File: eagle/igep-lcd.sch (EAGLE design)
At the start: 66 parts, among them IC1 LM1117IMPX-3.3, U1 SN74LVC8T245PW, U2 SN74LVC8T245PW, U3 SN74LVC8T245PW, U4 SN74LVC8T245PW

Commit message: Fixed one forgotten capacitor
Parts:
- removed C12: 0.1uF, rcl:C-EU050-025X075
- added C1: 100nF, rcl:C-EUC1206
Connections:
- net N$2: now also C1.2; no longer C12.2
- net N$3: now also C1.1; no longer C12.1
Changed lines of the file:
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@@
 <part name="U$5" library="lcd-bl" deviceset="LCD_BL" device=""/>
 <part name="U$6" library="ads7843" deviceset="ADS7843" device=""/>
-<part name="C12" library="rcl" deviceset="C-EU" device="050-025X075" value="0.1uF"/>
 <part name="C40" library="rcl" deviceset="C-EU" device="C1206" value="100nF"/>
 <part name="C16" library="rcl" deviceset="C-EU" device="C1206" value="100nF"/>
@@
 <part name="C11" library="rcl" deviceset="C-EU" device="C1206" value="10uF"/>
 <part name="C2" library="rcl" deviceset="C-EU" device="C1206" value="22uF"/>
+<part name="C1" library="rcl" deviceset="C-EU" device="C1206" value="100nF"/>
 </parts>
 <sheets>
@@
 <instance part="U$5" gate="G$1" x="208.28" y="-231.14" rot="MR270"/>
 <instance part="U$6" gate="G$1" x="106.68" y="-350.52"/>
-<instance part="C12" gate="G$1" x="132.08" y="121.92"/>
 <instance part="C40" gate="G$1" x="203.2" y="127" rot="R90"/>
 <instance part="C16" gate="G$1" x="205.74" y="124.46" rot="R90"/>
@@
 <instance part="C11" gate="G$1" x="48.26" y="71.12"/>
 <instance part="C2" gate="G$1" x="66.04" y="71.12"/>
+<instance part="C1" gate="G$1" x="132.08" y="121.92"/>
 </instances>
 <busses>
@@
 <wire x1="320.04" y1="81.28" x2="289.56" y2="81.28" width="0.1524" layer="91"/>
 <junction x="289.56" y="81.28"/>
-<pinref part="C12" gate="G$1" pin="1"/>
-<junction x="132.08" y="124.46"/>
 <pinref part="C39" gate="G$1" pin="1"/>
 <junction x="132.08" y="-5.08"/>
@@
 <junction x="132.08" y="60.96"/>
 <pinref part="C2" gate="G$1" pin="1"/>
+<pinref part="C1" gate="G$1" pin="1"/>
+<junction x="132.08" y="124.46"/>
 </segment>
 </net>
@@
 <wire x1="134.62" y1="35.56" x2="132.08" y2="35.56" width="0.1524" layer="91"/>
 <wire x1="132.08" y1="35.56" x2="132.08" y2="53.34" width="0.1524" layer="91"/>
-<pinref part="C12" gate="G$1" pin="2"/>
 <wire x1="134.62" y1="99.06" x2="132.08" y2="99.06" width="0.1524" layer="91"/>
 <wire x1="132.08" y1="99.06" x2="132.08" y2="116.84" width="0.1524" layer="91"/>
@@
 <pinref part="C11" gate="G$1" pin="2"/>
 <pinref part="C2" gate="G$1" pin="2"/>
-</segment>
-</net>
+<pinref part="C1" gate="G$1" pin="2"/>
+</segment>
+</net>

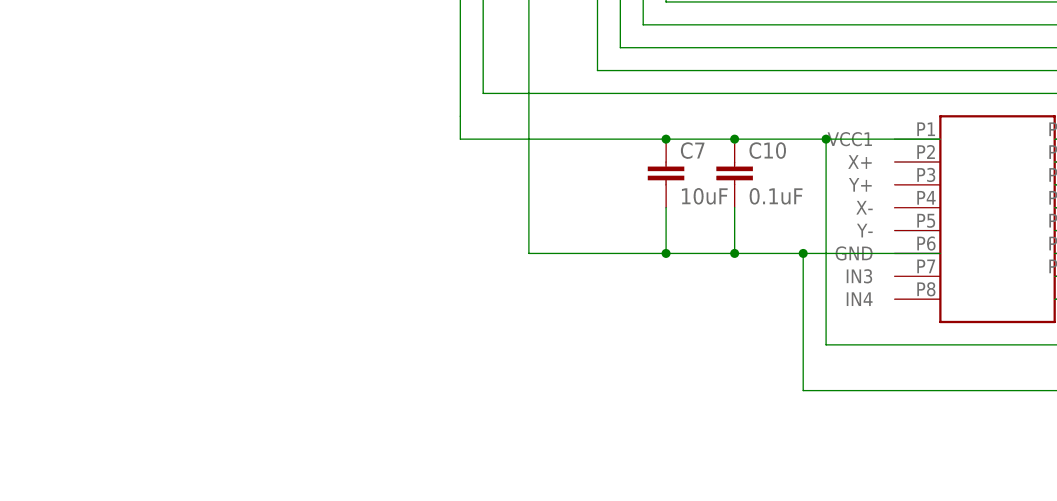
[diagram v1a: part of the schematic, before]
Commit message: Added TS connector eagle library Added TS connector to the schematic
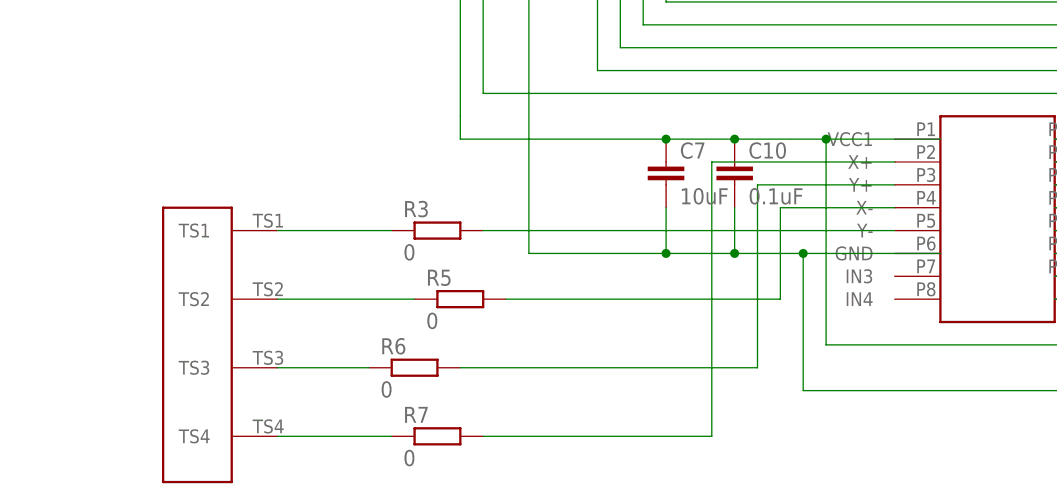
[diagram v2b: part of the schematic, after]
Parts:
- added R3, R5, R6, R7: 0, rcl:R-EU_R1206
- added U$7: TS_CON, ts_con:TS_CON
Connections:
- new net N$12: R3.2
- new net N$29: R3.1, U$7.TS1
- new net N$30: R5.2
- new net N$31: R5.1, U$7.TS2
- new net N$32: R6.2
- new net N$33: R6.1, U$7.TS3
- new net N$34: R7.1, U$7.TS4
- new net N$35: R7.2
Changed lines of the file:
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@@
 <part name="C2" library="rcl" deviceset="C-EU" device="C1206" value="22uF"/>
 <part name="C1" library="rcl" deviceset="C-EU" device="C1206" value="100nF"/>
+<part name="U$7" library="ts_con" deviceset="TS_CON" device=""/>
+<part name="R3" library="rcl" deviceset="R-EU_" device="R1206" value="0"/>
+<part name="R5" library="rcl" deviceset="R-EU_" device="R1206" value="0"/>
+<part name="R6" library="rcl" deviceset="R-EU_" device="R1206" value="0"/>
+<part name="R7" library="rcl" deviceset="R-EU_" device="R1206" value="0"/>
 </parts>
 <sheets>
@@
 <instance part="C2" gate="G$1" x="66.04" y="71.12"/>
 <instance part="C1" gate="G$1" x="132.08" y="121.92"/>
+<instance part="U$7" gate="G$1" x="17.78" y="-373.38" rot="R270"/>
+<instance part="R3" gate="G$1" x="43.18" y="-347.98"/>
+<instance part="R5" gate="G$1" x="45.72" y="-355.6"/>
+<instance part="R6" gate="G$1" x="40.64" y="-363.22"/>
+<instance part="R7" gate="G$1" x="43.18" y="-370.84"/>
 </instances>
 <busses>
@@
 </segment>
 </net>
+<net name="N$12" class="0">
+<segment>
+<wire x1="93.98" y1="-347.98" x2="48.26" y2="-347.98" width="0.1524" layer="91"/>
+<pinref part="R3" gate="G$1" pin="2"/>
+</segment>
+</net>
+<net name="N$29" class="0">
+<segment>
+<pinref part="U$7" gate="G$1" pin="TS1"/>
+<pinref part="R3" gate="G$1" pin="1"/>
+<wire x1="38.1" y1="-347.98" x2="25.4" y2="-347.98" width="0.1524" layer="91"/>
+</segment>
+</net>
+<net name="N$30" class="0">
+<segment>
+<wire x1="93.98" y1="-345.44" x2="81.28" y2="-345.44" width="0.1524" layer="91"/>
+<wire x1="81.28" y1="-345.44" x2="81.28" y2="-355.6" width="0.1524" layer="91"/>
+<wire x1="81.28" y1="-355.6" x2="50.8" y2="-355.6" width="0.1524" layer="91"/>
+<pinref part="R5" gate="G$1" pin="2"/>
+</segment>
+</net>
+<net name="N$31" class="0">
+<segment>
+<pinref part="U$7" gate="G$1" pin="TS2"/>
+<wire x1="40.64" y1="-355.6" x2="25.4" y2="-355.6" width="0.1524" layer="91"/>
+<pinref part="R5" gate="G$1" pin="1"/>
+</segment>
+</net>
+<net name="N$32" class="0">
+<segment>
+<wire x1="93.98" y1="-342.9" x2="78.74" y2="-342.9" width="0.1524" layer="91"/>
+<wire x1="78.74" y1="-342.9" x2="78.74" y2="-363.22" width="0.1524" layer="91"/>
+<wire x1="78.74" y1="-363.22" x2="45.72" y2="-363.22" width="0.1524" layer="91"/>
+<pinref part="R6" gate="G$1" pin="2"/>
+</segment>
+</net>
+<net name="N$33" class="0">
+<segment>
+<pinref part="U$7" gate="G$1" pin="TS3"/>
+<pinref part="R6" gate="G$1" pin="1"/>
+<wire x1="25.4" y1="-363.22" x2="35.56" y2="-363.22" width="0.1524" layer="91"/>
+</segment>
+</net>
+<net name="N$34" class="0">
+<segment>
+<pinref part="U$7" gate="G$1" pin="TS4"/>
+<pinref part="R7" gate="G$1" pin="1"/>
+<wire x1="25.4" y1="-370.84" x2="38.1" y2="-370.84" width="0.1524" layer="91"/>
+</segment>
+</net>
+<net name="N$35" class="0">
+<segment>
+<wire x1="93.98" y1="-340.36" x2="73.66" y2="-340.36" width="0.1524" layer="91"/>
+<wire x1="73.66" y1="-340.36" x2="73.66" y2="-370.84" width="0.1524" layer="91"/>
+<pinref part="R7" gate="G$1" pin="2"/>
+<wire x1="73.66" y1="-370.84" x2="48.26" y2="-370.84" width="0.1524" layer="91"/>
+</segment>
+</net>

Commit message: Added lcd connector Fix connections @ schema
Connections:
- removed net N$35 (its old number): R7.2
- new net N$3: R7.2, U$6.X+
- net N$1: now also U$1.MCSPI1_CLK
- net N$12: now also U$6.Y-
- net N$30: now also U$6.X-
- net N$32: now also U$6.Y+
- net N$7: now also U$1.MCSPI1_CS0
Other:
- moved on the sheet: C1, C10, C13, C14, C16, C39, C40, C7

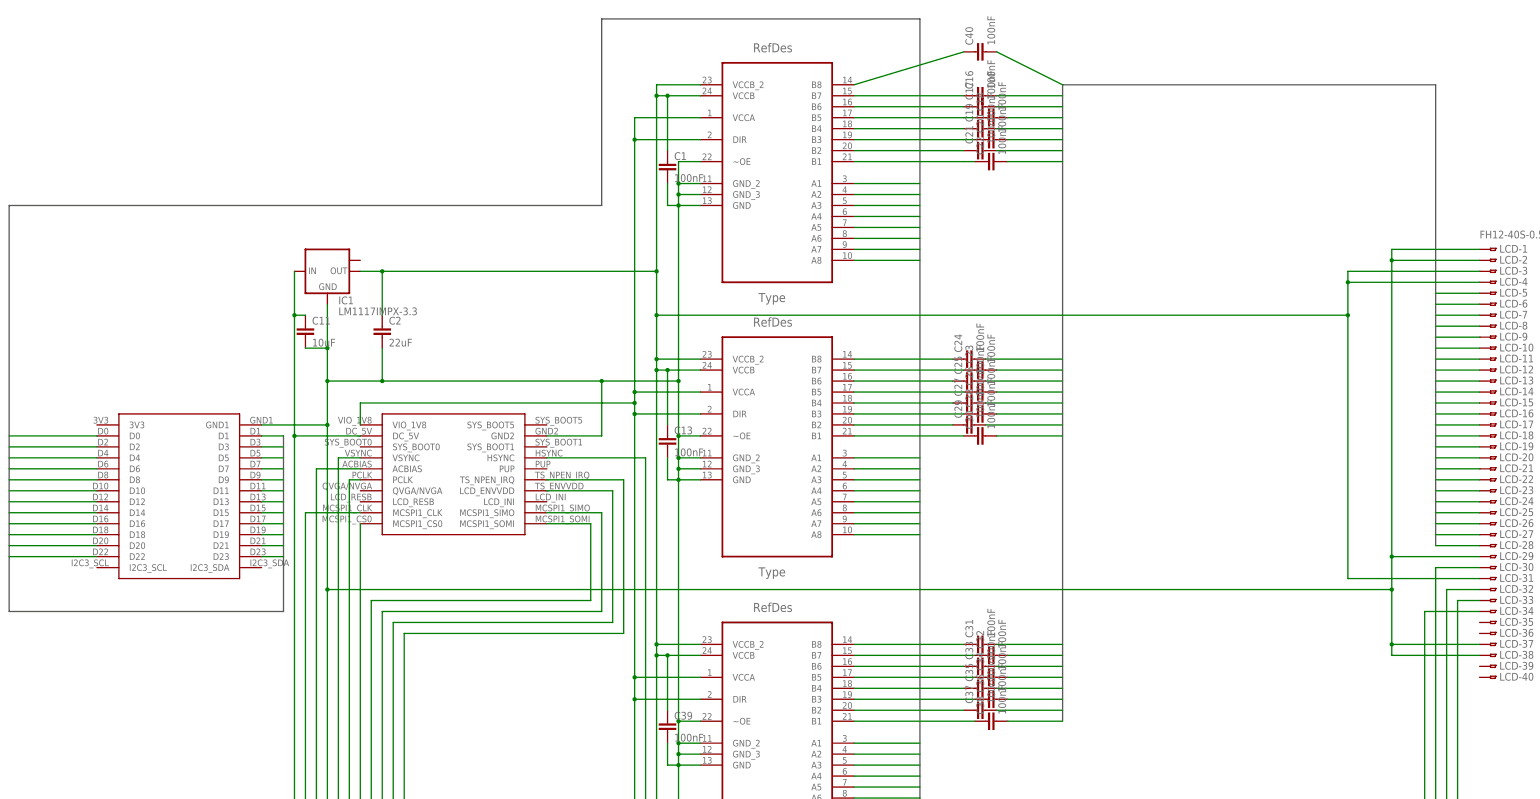
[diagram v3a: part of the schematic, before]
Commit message: Fixed ERC rules for bus
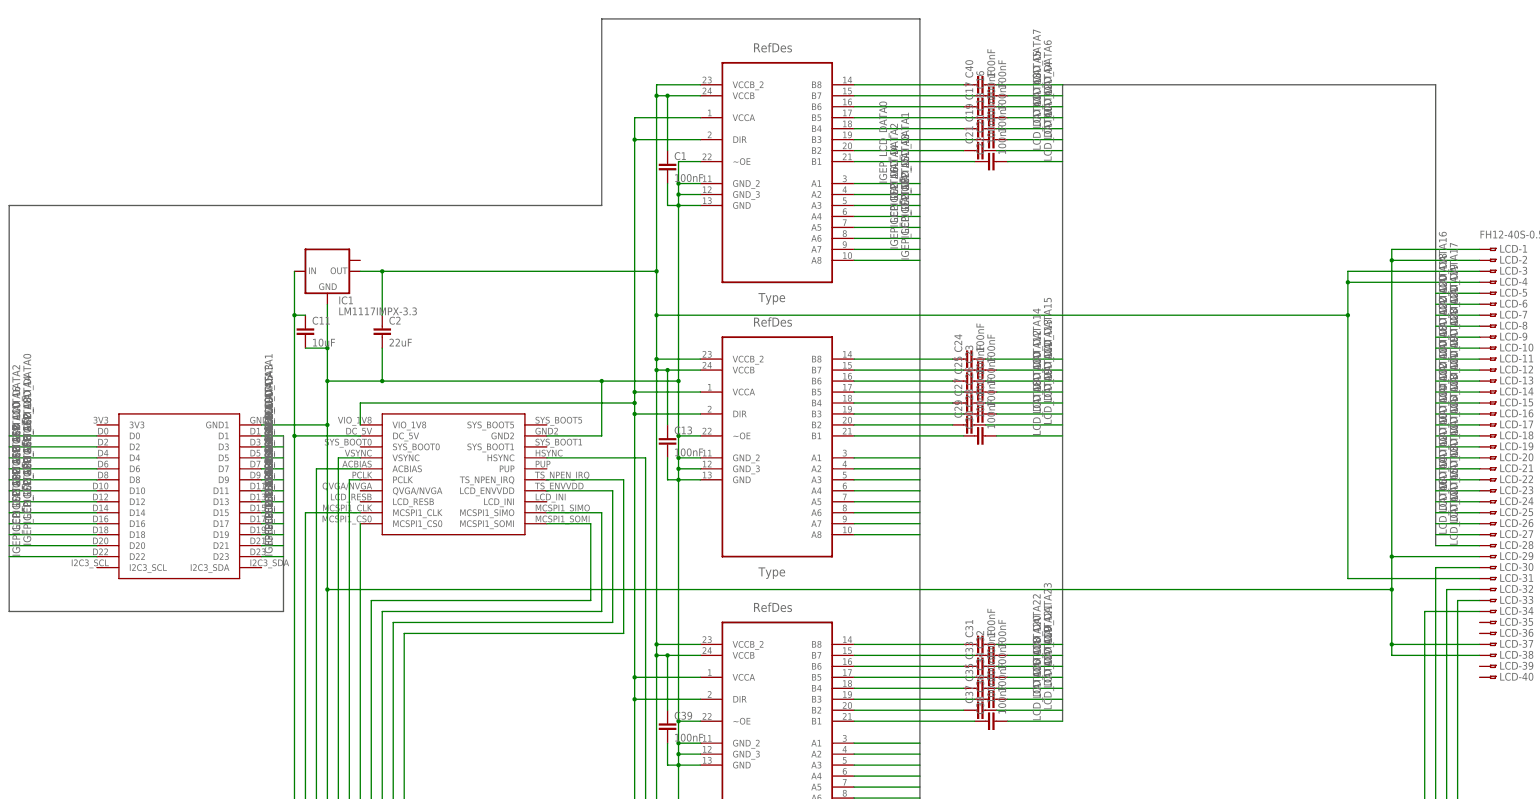
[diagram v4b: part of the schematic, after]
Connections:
- new net N$19: C40.1, U1.B8
- new net N$28: C24.1, U2.B8
- new net N$37: C16.1, U1.B7
- new net N$38: C17.1, U1.B6
- new net N$39: C18.1, U1.B5
- new net N$40: C19.1, U1.B4
- new net N$41: C20.1, U1.B3
- new net N$42: C21.1, U1.B2
- new net N$43: C22.1, U1.B1
- new net N$44: C23.1, U2.B7
- new net N$45: C25.1, U2.B6
- new net N$46: C26.1, U2.B5
- new net N$48: C28.1, U2.B3
- new net N$49: C29.1, U2.B2
- new net N$50: C30.1, U2.B1
- new net N$51: C31.1, U3.B8
- new net N$52: C32.1, U3.B7
- new net N$53: C33.1, U3.B6
- new net N$54: C34.1, U3.B5
- new net N$55: C35.1, U3.B4
- new net N$56: C36.1, U3.B3
- new net N$57: C37.1, U3.B2
- new net N$58: C38.1, U3.B1
- net LCD_DATA0: no longer C22.1, U1.B1
- net LCD_DATA1: no longer C21.1, U1.B2
- net LCD_DATA10: no longer C28.1, U2.B3
- net LCD_DATA12: no longer C26.1, U2.B5
- net LCD_DATA13: no longer C25.1, U2.B6
- net LCD_DATA14: no longer C23.1, U2.B7
- net LCD_DATA15: no longer C24.1, U2.B8
- net LCD_DATA16: no longer C38.1, U3.B1
- net LCD_DATA17: no longer C37.1, U3.B2
- net LCD_DATA18: no longer C36.1, U3.B3
- net LCD_DATA19: no longer C35.1, U3.B4
- net LCD_DATA2: no longer C20.1, U1.B3
- net LCD_DATA20: no longer C34.1, U3.B5
- net LCD_DATA21: no longer C33.1, U3.B6
- net LCD_DATA22: no longer C32.1, U3.B7
- net LCD_DATA23: no longer C31.1, U3.B8
- net LCD_DATA3: no longer C19.1, U1.B4
- net LCD_DATA4: no longer C18.1, U1.B5
- net LCD_DATA5: no longer C17.1, U1.B6
- net LCD_DATA6: no longer C16.1, U1.B7
- net LCD_DATA7: no longer C40.1, U1.B8
- net LCD_DATA8: no longer C30.1, U2.B1
- net LCD_DATA9: no longer C29.1, U2.B2
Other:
- moved on the sheet: C16, C40

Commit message: Added crosslinks on decoupling capacitors (to ease prototyping)
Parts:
- removed BL_5VOLT_1, BL_5VOLT_2, BL_5VOLT_3, BL_PWM_1, BL_PWM_2, BL_PWM_3: TPB1,27, testpad:TPB1,27
- added R10, R8, R9: 0, rcl:R-EU_R1206
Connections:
- removed net N$12: R3.2, U$6.Y-
- removed net N$18: BL_PWM_2.TP, U$3.EN
- removed net N$19: C40.1, U1.B8
- removed net N$24: BL_PWM_3.TP, U$4.EN
- removed net N$28: C24.1, U2.B8
- removed net N$3: R7.2, U$6.X+
- removed net N$30: R5.2, U$6.X-
- removed net N$32: R6.2, U$6.Y+
- removed net N$37: C16.1, U1.B7
- removed net N$38: C17.1, U1.B6
- removed net N$39: C18.1, U1.B5
- removed net N$40: C19.1, U1.B4
- removed net N$41: C20.1, U1.B3
- removed net N$42: C21.1, U1.B2
- removed net N$43: C22.1, U1.B1
- removed net N$44: C23.1, U2.B7
- removed net N$45: C25.1, U2.B6
- removed net N$46: C26.1, U2.B5
- removed net N$47: C27.1, U2.B4
- removed net N$48: C28.1, U2.B3
- removed net N$49: C29.1, U2.B2
- removed net N$50: C30.1, U2.B1
- removed net N$51: C31.1, U3.B8
- removed net N$52: C32.1, U3.B7
- removed net N$53: C33.1, U3.B6
- removed net N$54: C34.1, U3.B5
- removed net N$55: C35.1, U3.B4
- removed net N$56: C36.1, U3.B3
- removed net N$57: C37.1, U3.B2
- removed net N$58: C38.1, U3.B1
- removed net N$6: BL_PWM_1.TP, U$2.EN
- net LCD_DATA0: now also C22.1, U1.B1
- net LCD_DATA1: now also C21.1, U1.B2
- net LCD_DATA10: now also C28.1, U2.B3
- net LCD_DATA11: now also C27.1, U2.B4
- net LCD_DATA12: now also C26.1, U2.B5
- net LCD_DATA13: now also C25.1, U2.B6
- net LCD_DATA14: now also C23.1, U2.B7
- net LCD_DATA15: now also C24.1, U2.B8
- net LCD_DATA16: now also C38.1, U3.B1
- net LCD_DATA17: now also C37.1, U3.B2
- net LCD_DATA18: now also C36.1, U3.B3
- net LCD_DATA19: now also C35.1, U3.B4
- net LCD_DATA2: now also C20.1, U1.B3
- net LCD_DATA20: now also C34.1, U3.B5
- net LCD_DATA21: now also C33.1, U3.B6
- net LCD_DATA22: now also C32.1, U3.B7
- net LCD_DATA23: now also C31.1, U3.B8
- net LCD_DATA3: now also C19.1, U1.B4
- net LCD_DATA4: now also C18.1, U1.B5
- net LCD_DATA5: now also C17.1, U1.B6
- net LCD_DATA6: now also C16.1, U1.B7
- net LCD_DATA7: now also C40.1, U1.B8
- net LCD_DATA8: now also C30.1, U2.B1
- net LCD_DATA9: now also C29.1, U2.B2
- net N$29: now also R3.2, U$6.Y-
- net N$31: now also R5.2, U$6.X-
- net N$33: now also R6.2, U$6.Y+
- net N$34: now also R7.2, U$6.X+
- net N$35: now also R10.1, R10.2, R8.1, R8.2, R9.1, R9.2, U$2.EN, U$3.EN, U$4.EN; no longer BL_5VOLT_1.TP, BL_5VOLT_2.TP, BL_5VOLT_3.TP
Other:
- moved on the sheet: R3, R5, R6, R7
